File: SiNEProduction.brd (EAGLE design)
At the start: 80 x 60 mm, 35 parts, among them IC1 74HCT164D, IC3 ATTINY24/44/84-SSU, J1 AVR_SPI_PRG_6NS

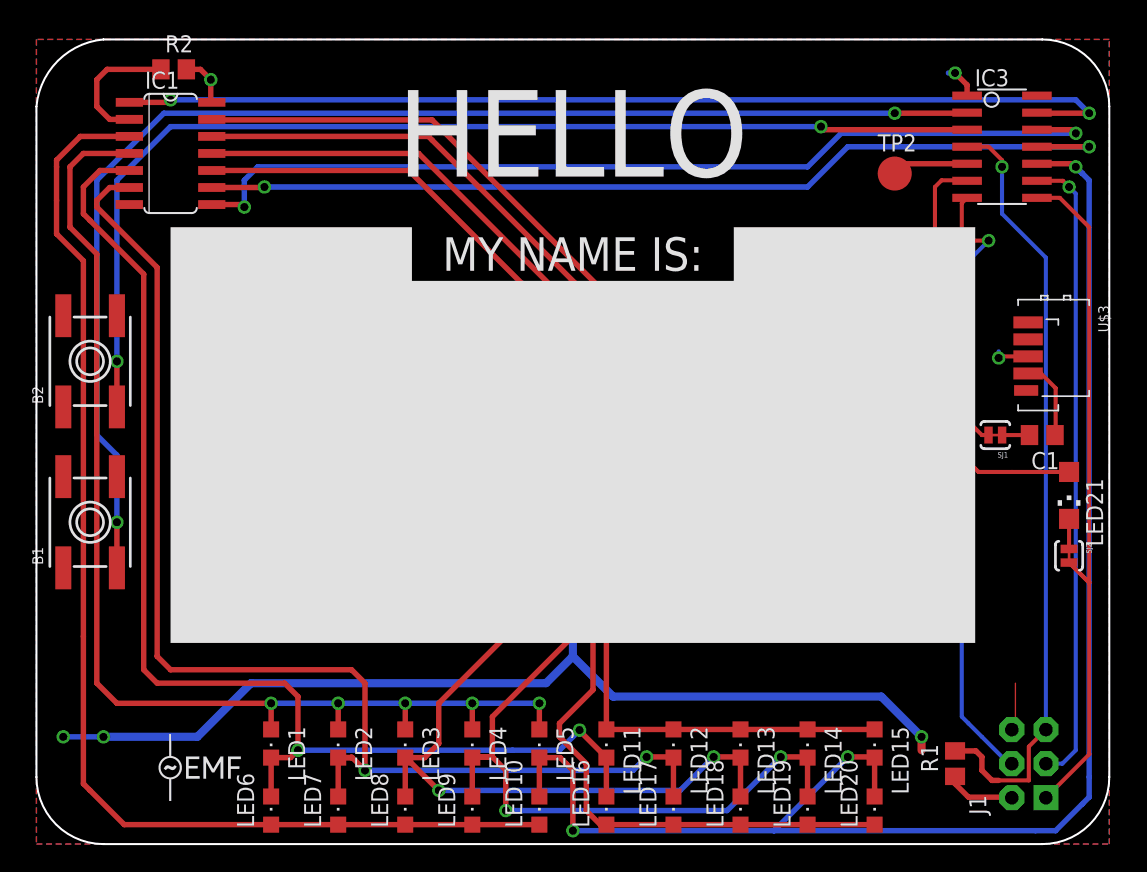
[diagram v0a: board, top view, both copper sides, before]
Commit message: Swapped sides for one button and IR Receiver Added bottom silk screen Added posible holle for Pin
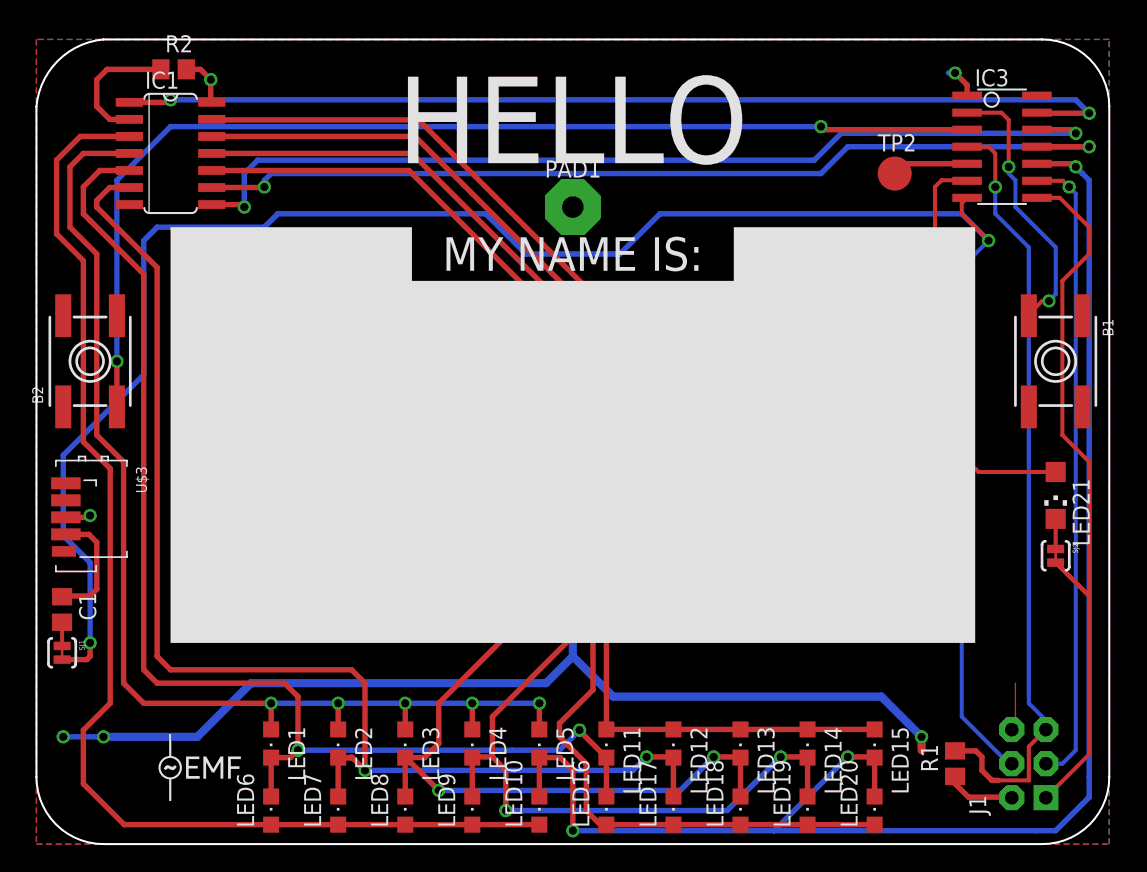
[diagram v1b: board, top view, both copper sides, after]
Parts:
- added PAD1: WIREPAD4,16O1,6, wirepad:4,16O1,6
- moved C1 74.2 mm to (1.92, 17.5), turned to 270 degrees
- moved B1 73.0 mm to (76.0, 36.0), turned to 270 degrees
- moved U$3 72.7 mm to (4.25, 25.0)
- moved SJ1 71.5 mm to (1.92, 14.3), turned to 270 degrees
- moved LED21 1.00 mm to (76.0, 26.0)
- moved SJ2 1.00 mm to (76.0, 21.5)
- turned BAT2 to 180 degrees
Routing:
- net MOSI: track 62.6 -> 149.5 mm, vias 1 -> 2
- net BTN1: track 96.5 -> 20.5 mm
- net MISO: track 52.9 -> 57.4 mm
- net N$6: track 6.09 -> 8.87 mm
- net LED_C4: track 105.5 -> 103.7 mm
- net LED_R2: track 88.8 -> 90.4 mm
- net LED_R1: track 87.5 -> 86.4 mm
- net IR_PWM: track 32.0 -> 31.0 mm
- net VCC: track 14.4 -> 13.6 mm
- net LED_R4: track 95.3 -> 94.7 mm
- net LED_R3: track 87.3 -> 86.7 mm
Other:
- board text added: "@CharlesYarnold"
- board text added: "@dpslwk"
- board text added: "@thinkl33t"
- board text added: "Built by:"
- board text added: "Ciseco"
- board text added: "Design by:"
- board text added: "Electromagnetic Wave"
- board text added: "SiNE Badge"
- board text added: "Sunday 5th May 2013"
- board text added: "www.emfcamp.org/wave"

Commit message: Adding Logo's
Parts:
- added U$1: (no value), SiNE Parts:TWILIO
- added U$5: (no value), SiNE Parts:CISECO1
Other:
- board text added: "SiNE"
- board text removed: "Ciseco"
- board text removed: "SiNE Badge"

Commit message: Inverted MY NAME IS:
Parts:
- added U$4: (no value), SiNE Parts:NAME
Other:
- board text removed: "MY NAME IS:"
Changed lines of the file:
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@@
 <setting verticaltext="up"/>
 </settings>
-<grid distance="1" unitdist="mm" unit="mm" style="lines" multiple="1" display="yes" altdistance="0.5" altunitdist="mm" altunit="mm"/>
+<grid distance="39.3701" unitdist="mil" unit="mil" style="lines" multiple="1" display="yes" altdistance="0.5" altunitdist="mm" altunit="mm"/>
 <layers>
 <layer number="1" name="Top" color="4" fill="1" visible="yes" active="yes"/>
@@
 <vertex x="70" y="15"/>
 </polygon>
-<text x="40" y="44" size="2.5" layer="21" font="vector" ratio="15" align="center">MY NAME IS:</text>
 <circle x="40" y="22" radius="9" width="0" layer="42"/>
 <text x="62" y="41" size="2.54" layer="22" font="vector" ratio="15" rot="MR0">Electromagnetic Wave</text>
@@
 <element name="U$1" library="SiNE Parts" package="TWILIO" value="" x="60" y="1" rot="MR0"/>
 <element name="U$5" library="SiNE Parts" package="CISECO1" value="" x="22" y="15" rot="MR0"/>
+<element name="U$4" library="SiNE Parts" package="NAME" value="" x="40" y="44"/>
 </elements>
 <signals>

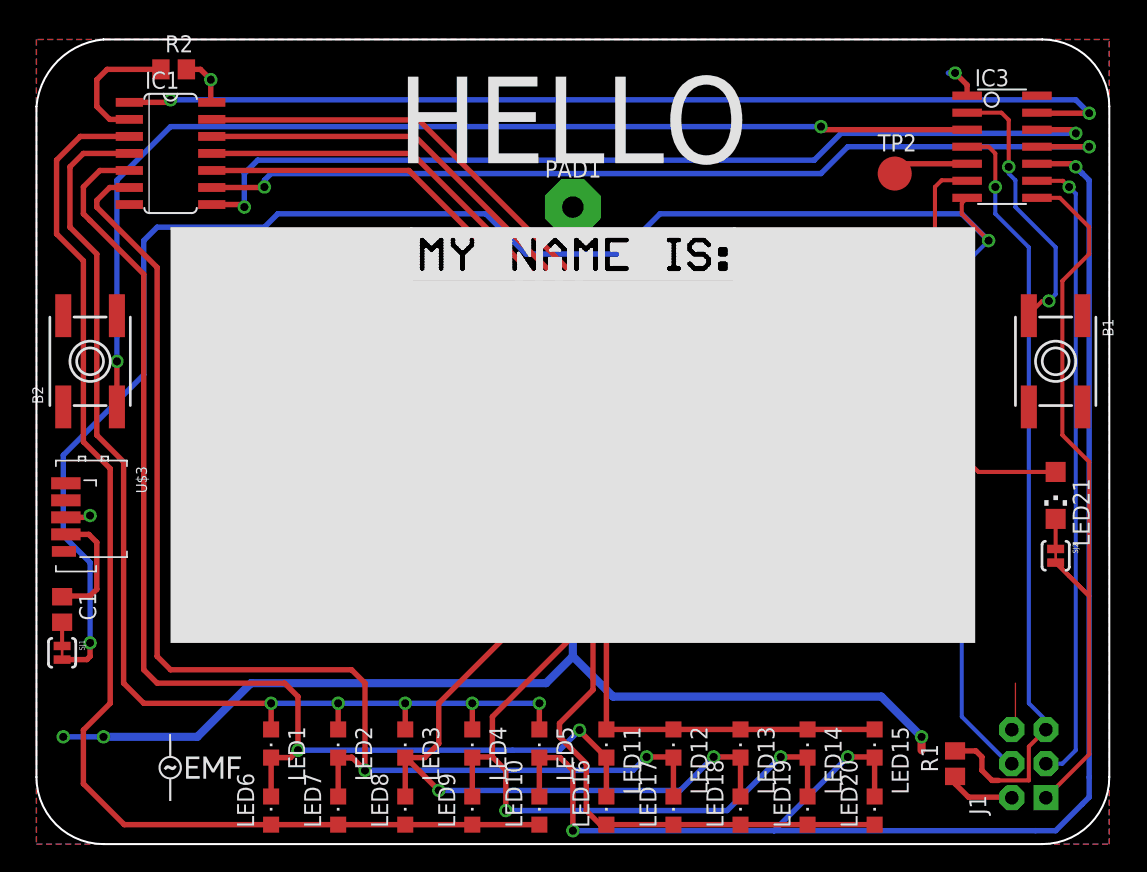
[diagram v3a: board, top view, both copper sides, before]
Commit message: Labeled LED's
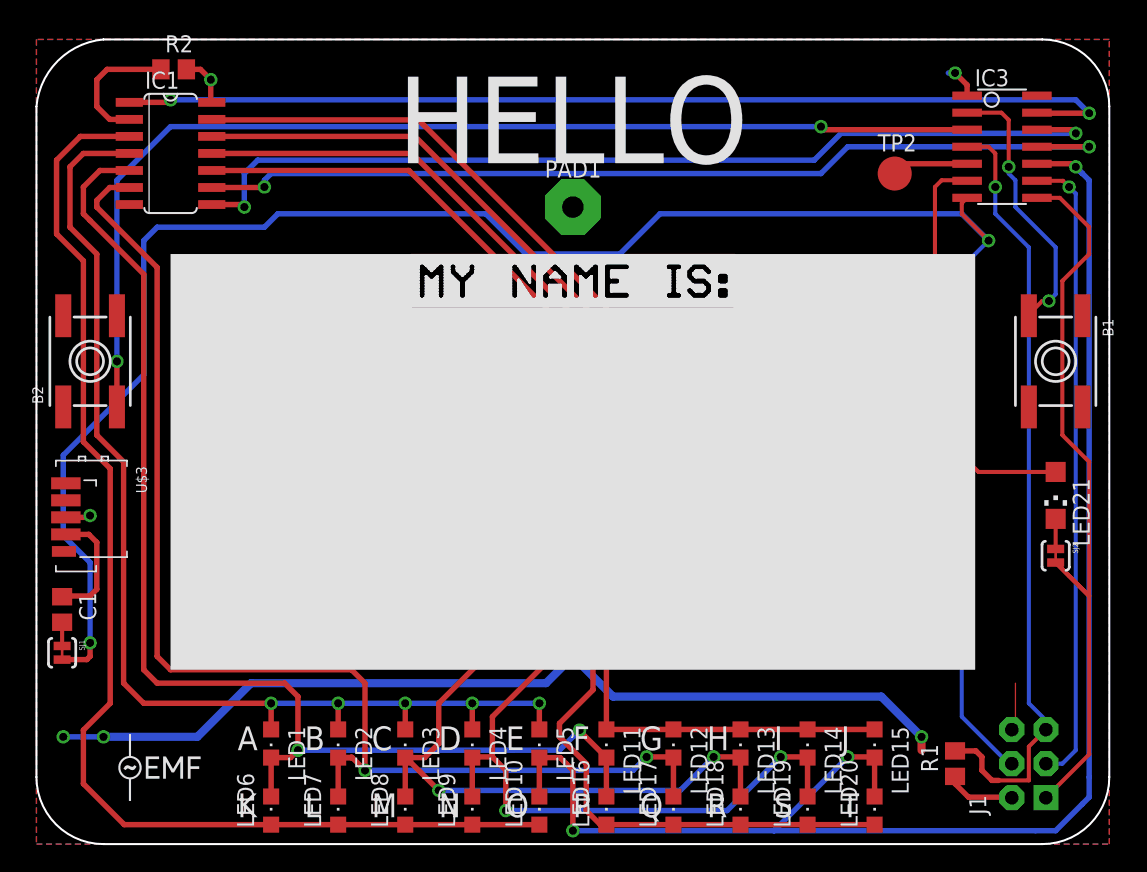
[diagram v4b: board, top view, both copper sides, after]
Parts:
- moved U$2 3.00 mm to (6.00, 3.00)
- moved U$4 2.00 mm to (40.0, 42.0)
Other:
- board text added: "A"
- board text added: "B"
- board text added: "C"
- board text added: "D"
- board text added: "E"
- board text added: "F"
- board text added: "G"
- board text added: "H"
- board text added: "I"
- board text added: "J"
- board text added: "K"
- board text added: "L"
- board text added: "M"
- board text added: "N"
- board text added: "O"
- board text added: "P"
- board text added: "Q"
- board text added: "R"
- board text added: "S"
- board text added: "T"

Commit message: Adding Fiducials
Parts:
- added JP1, JP2, JP3: FIDUCIAL1X2.5-STOP, CISECO eaglecad designs:FIDUCIAL-1X2.5-STOP
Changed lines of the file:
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@@
 <setting verticaltext="up"/>
 </settings>
-<grid distance="1" unitdist="mm" unit="mm" style="lines" multiple="1" display="yes" altdistance="0.5" altunitdist="mm" altunit="mm"/>
+<grid distance="1" unitdist="mm" unit="mm" style="lines" multiple="1" display="yes" altdistance="0.1" altunitdist="mm" altunit="mm"/>
 <layers>
 <layer number="1" name="Top" color="4" fill="1" visible="yes" active="yes"/>
@@
 <layer number="27" name="tValues" color="7" fill="1" visible="no" active="yes"/>
 <layer number="28" name="bValues" color="7" fill="1" visible="no" active="yes"/>
-<layer number="29" name="tStop" color="7" fill="3" visible="no" active="yes"/>
+<layer number="29" name="tStop" color="7" fill="3" visible="yes" active="yes"/>
 <layer number="30" name="bStop" color="7" fill="6" visible="no" active="yes"/>
 <layer number="31" name="tCream" color="7" fill="4" visible="no" active="yes"/>
@@
 <layer number="111" name="MPL" color="7" fill="1" visible="yes" active="yes"/>
 <layer number="112" name="tSilk" color="7" fill="1" visible="yes" active="yes"/>
+<layer number="113" name="Stencile_Ref" color="11" fill="1" visible="no" active="yes"/>
 <layer number="116" name="Patch_BOT" color="9" fill="4" visible="yes" active="yes"/>
 <layer number="118" name="Rect_Pads" color="4" fill="1" visible="yes" active="yes"/>
@@
 <board>
 <plain>
+<wire x1="80" y1="55" x2="80" y2="5" width="0.15" layer="20"/>
+<wire x1="80" y1="5" x2="75" y2="0" width="0.15" layer="20" curve="-90"/>
+<wire x1="75" y1="0" x2="5" y2="0" width="0.15" layer="20"/>
+<wire x1="5" y1="0" x2="0" y2="5" width="0.15" layer="20" curve="-90"/>
 <wire x1="0" y1="5" x2="0" y2="55" width="0.15" layer="20"/>
+<wire x1="0" y1="55" x2="5" y2="60" width="0.15" layer="20" curve="-90"/>
 <wire x1="5" y1="60" x2="75" y2="60" width="0.15" layer="20"/>
-<wire x1="80" y1="55" x2="80" y2="5" width="0.15" layer="20"/>
-<wire x1="75" y1="0" x2="5" y2="0" width="0.15" layer="20"/>
-<wire x1="0" y1="5" x2="5" y2="0" width="0.15" layer="20" curve="90"/>
-<wire x1="75" y1="0" x2="80" y2="5" width="0.15" layer="20" curve="90"/>
 <wire x1="75" y1="60" x2="80" y2="55" width="0.15" layer="20" curve="-90"/>
-<wire x1="5" y1="60" x2="0" y2="55" width="0.15" layer="20" curve="79.611142"/>
 <text x="40" y="54" size="6.4516" layer="21" font="vector" ratio="15" align="center">HELLO</text>
 <polygon width="0" layer="21">
@@
 <element name="U$5" library="SiNE Parts" package="CISECO1" value="" x="22" y="15" rot="MR0"/>
 <element name="U$4" library="SiNE Parts" package="NAME" value="" x="40" y="41.999996875"/>
+<element name="JP1" library="CISECO eaglecad designs" package="FIDUCIAL-1X2.5-STOP" value="FIDUCIAL1X2.5-STOP" x="65.5" y="3"/>
+<element name="JP2" library="CISECO eaglecad designs" package="FIDUCIAL-1X2.5-STOP" value="FIDUCIAL1X2.5-STOP" x="16" y="57"/>
+<element name="JP3" library="CISECO eaglecad designs" package="FIDUCIAL-1X2.5-STOP" value="FIDUCIAL1X2.5-STOP" x="3" y="11.3"/>
 </elements>
 <signals>
